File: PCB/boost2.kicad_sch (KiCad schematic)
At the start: 18 parts, among them Q2 G1003B-23, U8 LM3478MA

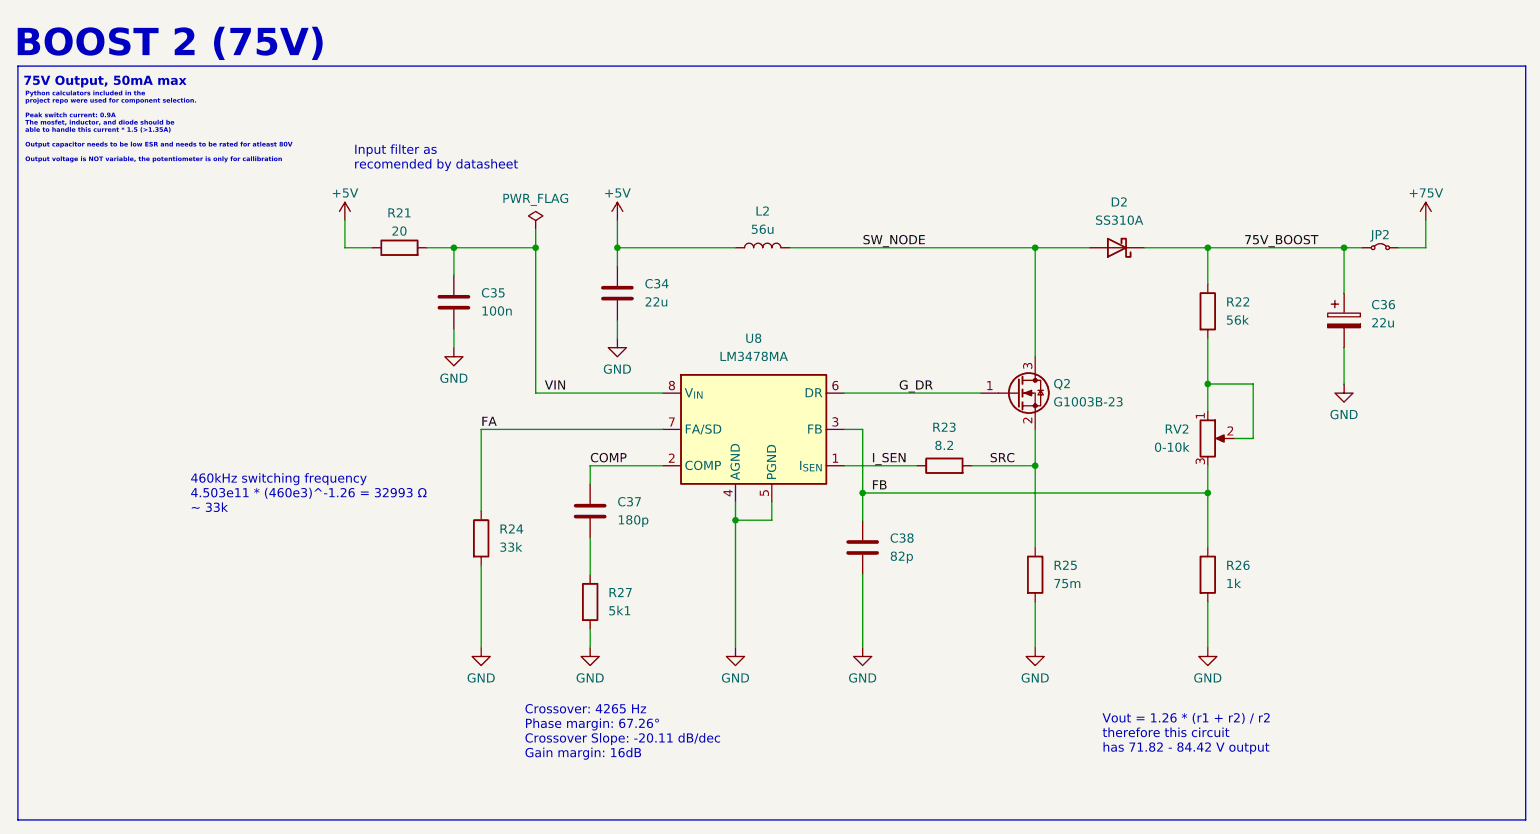
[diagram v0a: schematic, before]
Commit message: Fixed floating boot0
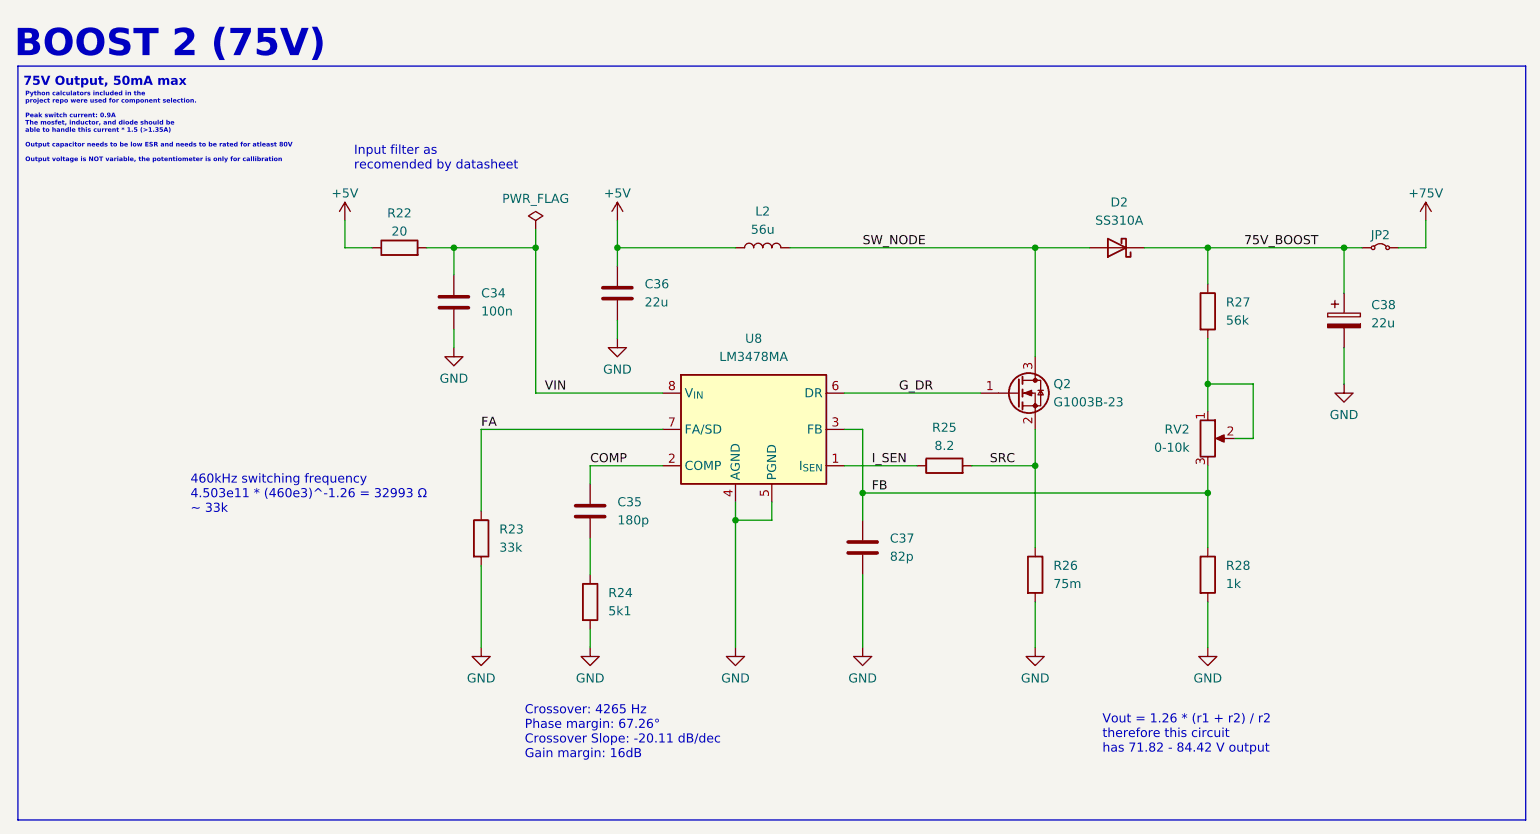
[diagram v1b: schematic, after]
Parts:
- renumbered C35 to C34, C37 to C35, C34 to C36, C38 to C37, C36 to C38, R21 to R22, R24 to R23, R27 to R24, R23 to R25, R25 to R26, R22 to R27, R26 to R28
